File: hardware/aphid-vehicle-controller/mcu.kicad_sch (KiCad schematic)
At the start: 2 parts, among them J2 Conn_ST_STDC14, U1 STM32F405RGTx

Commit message: worked on schematic
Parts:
- added Y1: Crystal, symbol Device:Crystal
- J2: value Conn_ST_STDC14 -> MAIN_DEBUG
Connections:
- net GND: now reaches J2.11 (GNDDetect)
- net GND: now also J2.5 (GND), J2.7 (GND)
- net MAIN_NRST: now reaches J2.12 (~{RST})
- net MAIN_DBG_RX: now reaches J2.13 (VCP_RX)
- net MAIN_DBG_TX: now reaches J2.14 (VCP_TX)
- net +3.3V: now reaches J2.3 (VCC)
- net MAIN_SWDIO: now reaches J2.4 (JTMS/SWDIO)
- net MAIN_SWCLK: now reaches J2.6 (JCLK/SWCLK)
- net MAIN_SWO: now reaches J2.8 (JTDO/SWO)

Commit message: more work on pcb
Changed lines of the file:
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@@
+		)
+	)
+	(hierarchical_label "POWER_KEEPALIVE"
+		(shape output)
+		(at 217.17 43.18 0)
+		(fields_autoplaced yes)
+		(effects
+			(font
+				(size 1.27 1.27)
+			)
+			(justify left)
 		)
 	)

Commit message: worked on VCM
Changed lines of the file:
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@@
 		)
 	)
-	(hierarchical_label "ACC2_FILTERED"
+	(hierarchical_label "DIR_R"
 		(shape input)
-		(at 190.5 138.43 0)
+		(at 182.88 118.11 0)
+		(fields_autoplaced yes)
+		(effects
+			(font
+				(size 1.27 1.27)
+			)
+			(justify left)
+		)
+	)
+	(hierarchical_label "MONITOR_UART_TX"
+		(shape output)
+		(at 45.72 92.71 0)
+		(fields_autoplaced yes)
+		(effects
+			(font
+				(size 1.27 1.27)
+			)
+			(justify left)
+		)
+	)
+	(hierarchical_label "MONITOR_UART_RX"
+		(shape input)
+		(at 45.72 96.52 0)
+		(fields_autoplaced yes)
+		(effects
+			(font
+				(size 1.27 1.27)
+			)
+			(justify left)
+		)
+	)
+	(hierarchical_label "BRAKE"
+		(shape input)
+		(at 182.88 106.68 0)
+		(fields_autoplaced yes)
+		(effects
+			(font
+				(size 1.27 1.27)
+			)
+			(justify left)
+		)
+	)
+	(hierarchical_label "CRANK_SENSE"
+		(shape input)
+		(at 195.58 130.81 0)
 		(fields_autoplaced yes)
 		(effects
@@
 		(shape output)
 		(at 217.17 43.18 0)
+		(fields_autoplaced yes)
+		(effects
+			(font
+				(size 1.27 1.27)
+			)
+			(justify left)
+		)
+	)
+	(hierarchical_label "DIR_F"
+		(shape input)
+		(at 182.88 113.03 0)
 		(fields_autoplaced yes)
 		(effects
@@
 		)
 	)
-	(hierarchical_label "UPPER_CONTACTOR_ENABLE"
-		(shape output)
-		(at 201.93 114.3 0)
-		(fields_autoplaced yes)
-		(effects
-			(font
-				(size 1.27 1.27)
-			)
-			(justify left)
-		)
-	)
 	(hierarchical_label "CAN1_RX"
 		(shape input)
@@
 		)
 	)
-	(hierarchical_label "ACC1_FILTERED"
+	(hierarchical_label "ACC"
 		(shape input)
 		(at 176.53 91.44 0)
@@
 		)
 	)
-	(hierarchical_label "LOWER_CONTACTOR_ENABLE"
-		(shape output)
-		(at 201.93 116.84 0)
+	(hierarchical_label "IGNITION_SENSE"
+		(shape input)
+		(at 215.9 116.84 0)
 		(fields_autoplaced yes)
 		(effects
@@
 		)
 	)
-	(hierarchical_label "PRECHARGE_ENABLE"
-		(shape output)
-		(at 203.2 109.22 0)
+	(hierarchical_label "VIN_SENSE"
+		(shape input)
+		(at 215.9 114.3 0)
 		(fields_autoplaced yes)
 		(effects

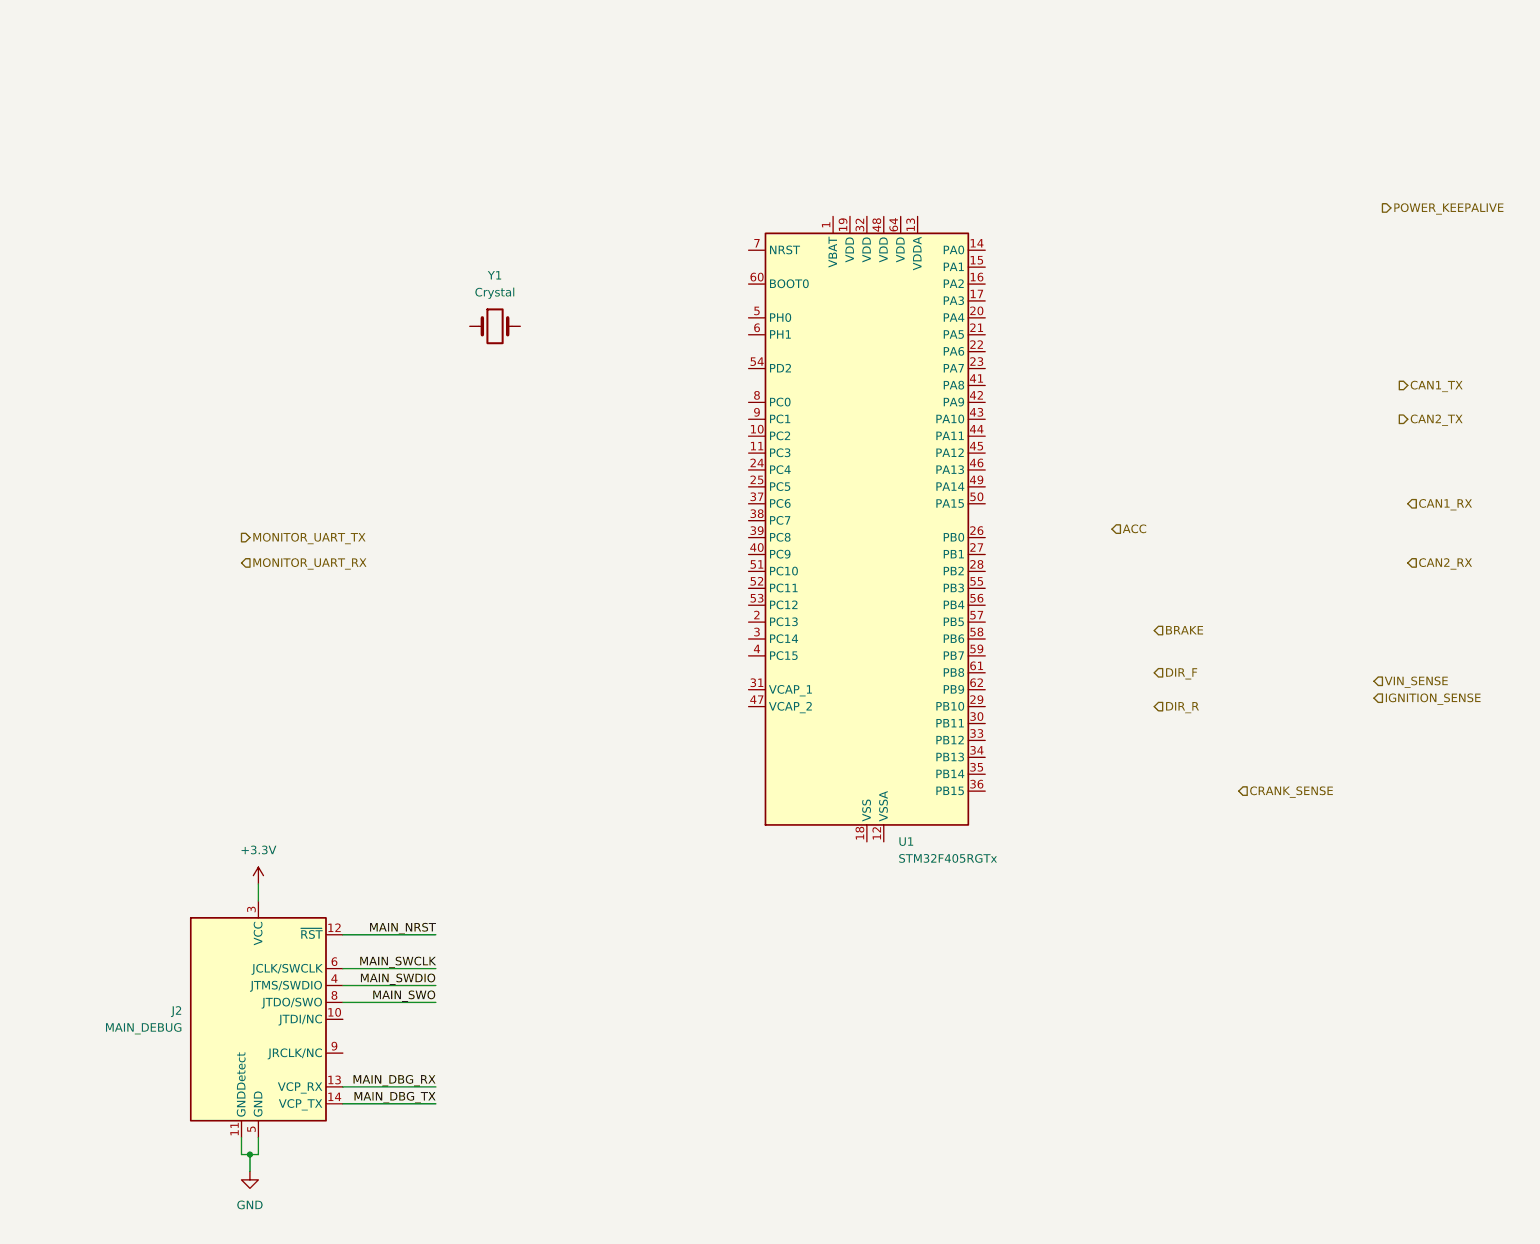
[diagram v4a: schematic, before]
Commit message: feat: changed to STM32G4xx series MCU
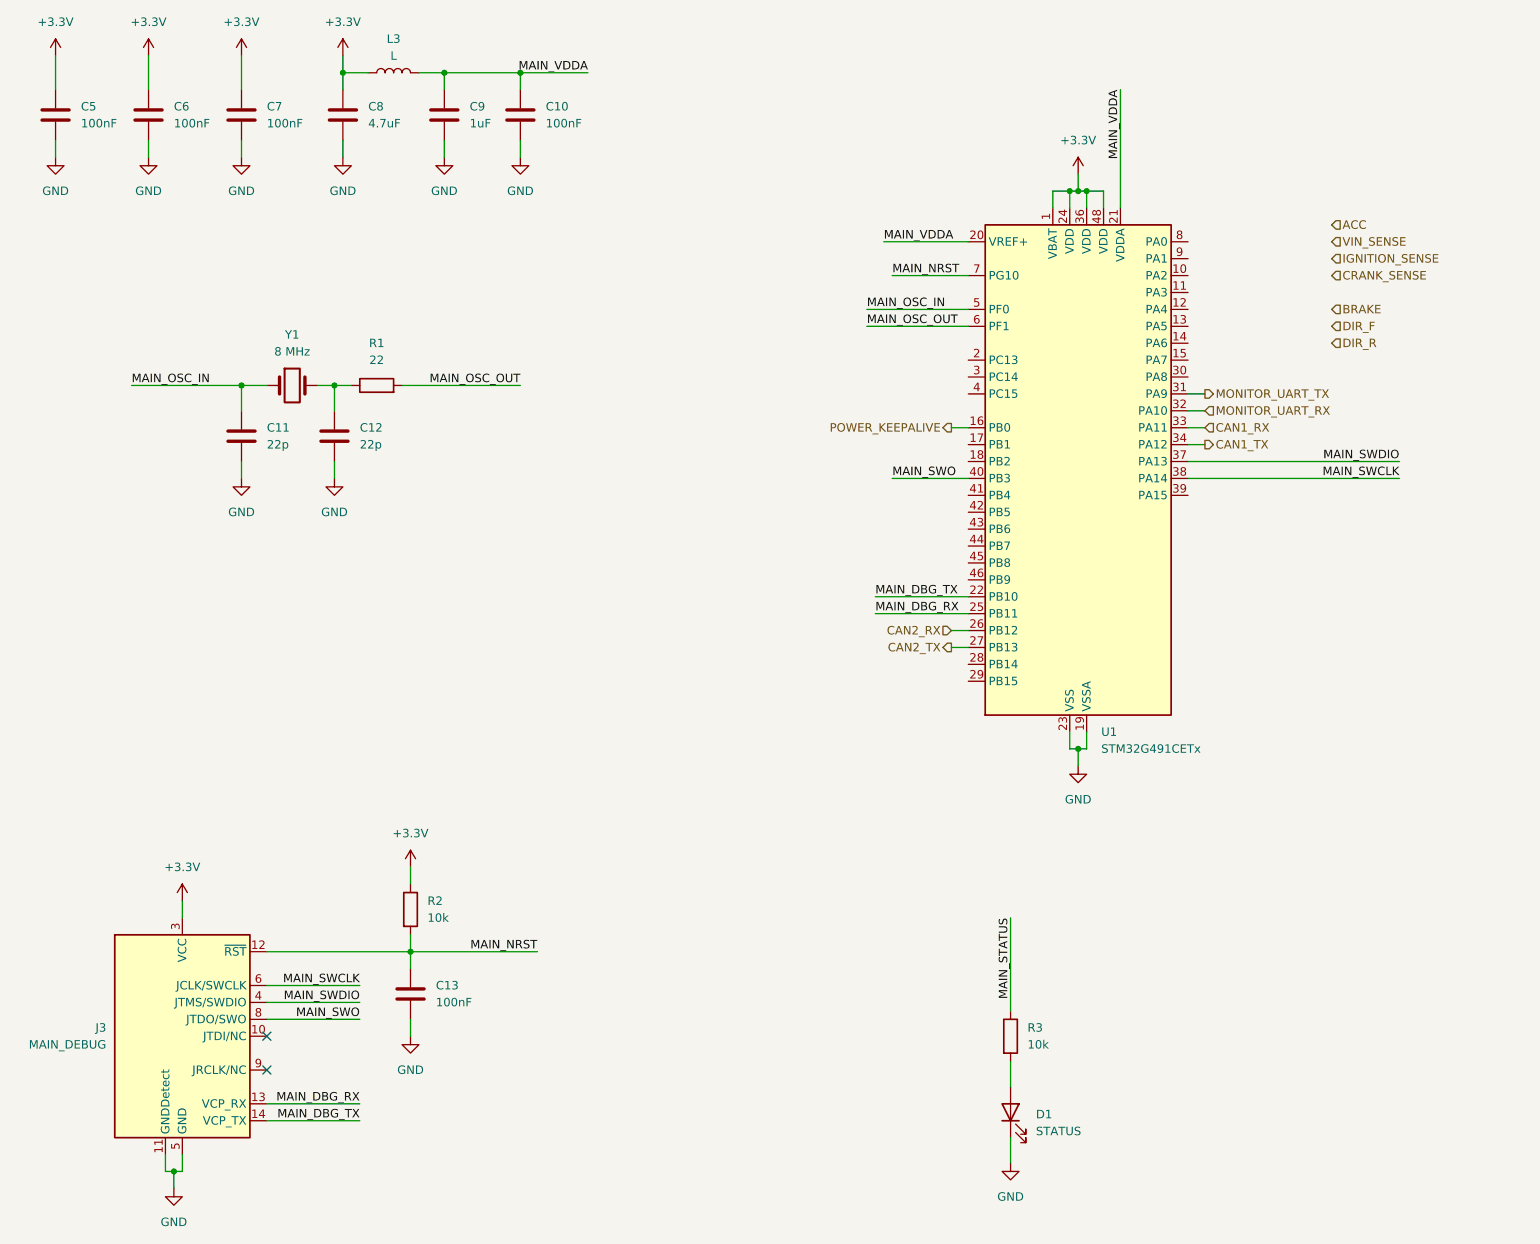
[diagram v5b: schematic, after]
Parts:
- removed U1: STM32F405RGTx, Package_QFP:LQFP-64_10x10mm_P0.5mm, symbol MCU_ST_STM32F4:STM32F405RGTx
- added C10, C13, C5, C6, C7: 100nF, Capacitor_SMD:C_0603_1608Metric, symbol Device:C
- added C11, C12: 22p, Capacitor_SMD:C_0603_1608Metric, symbol Device:C
- added C8: 4.7uF, Capacitor_SMD:C_0805_2012Metric, symbol Device:C
- added C9: 1uF, Capacitor_SMD:C_0603_1608Metric, symbol Device:C
- added D1: STATUS, LED_SMD:LED_0603_1608Metric, symbol Device:LED
- added L3: L, Inductor_SMD:L_0805_2012Metric, symbol Device:L
- added R1: 22, Resistor_SMD:R_0603_1608Metric, symbol Device:R
- added R2, R3: 10k, Resistor_SMD:R_0603_1608Metric, symbol Device:R
- added U1: STM32G491CETx, Package_QFP:LQFP-48_7x7mm_P0.5mm, symbol MCU_ST_STM32G4:STM32G491CETx
- Y1: value Crystal -> 8 MHz; footprint (none) -> aphid:ABM3-x.xxxMHZ-D2Y-T
- renumbered J2 to J3
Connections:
- net +3.3V: now also C5.1, C6.1, C7.1, C8.1, L3.1, R2.1, U1.1 (VBAT), U1.24 (VDD), U1.36 (VDD), U1.48 (VDD)
- net CAN1_RX: now also U1.33 (PA11)
- net CAN1_TX: now also U1.34 (PA12)
- net CAN2_RX: now also U1.26 (PB12)
- net CAN2_TX: now also U1.27 (PB13)
- net GND: now also C10.2, C11.2, C12.2, C13.2, C5.2, C6.2, C7.2, C8.2, C9.2, D1.1 (K), U1.19 (VSSA), U1.23 (VSS), U1.35 (VSS), U1.47 (VSS)
- net MAIN_DBG_RX: now also U1.25 (PB11)
- net MAIN_DBG_TX: now also U1.22 (PB10)
- net MAIN_NRST: now also C13.1, R2.2, U1.7 (PG10)
- net MAIN_SWCLK: now also U1.38 (PA14)
- net MAIN_SWDIO: now also U1.37 (PA13)
- net MAIN_SWO: now also U1.40 (PB3)
- net MONITOR_UART_RX: now also U1.32 (PA10)
- net MONITOR_UART_TX: now also U1.31 (PA9)
- net POWER_KEEPALIVE: now also U1.16 (PB0)
- net MAIN_OSC_IN: now reaches Y1.1
- net MAIN_OSC_IN: now also C11.1, U1.5 (PF0)
- net at Y1.2: now also C12.1, R1.1
- new net: D1.2 (A), R3.2
- new net MAIN_OSC_OUT: R1.2, U1.6 (PF1)
- new net MAIN_STATUS: R3.1
- new net MAIN_VDDA: C10.1, C9.1, L3.2, U1.20 (VREF+), U1.21 (VDDA)
- no-connect marks 0 -> 2
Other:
- moved on the sheet: J3, Y1

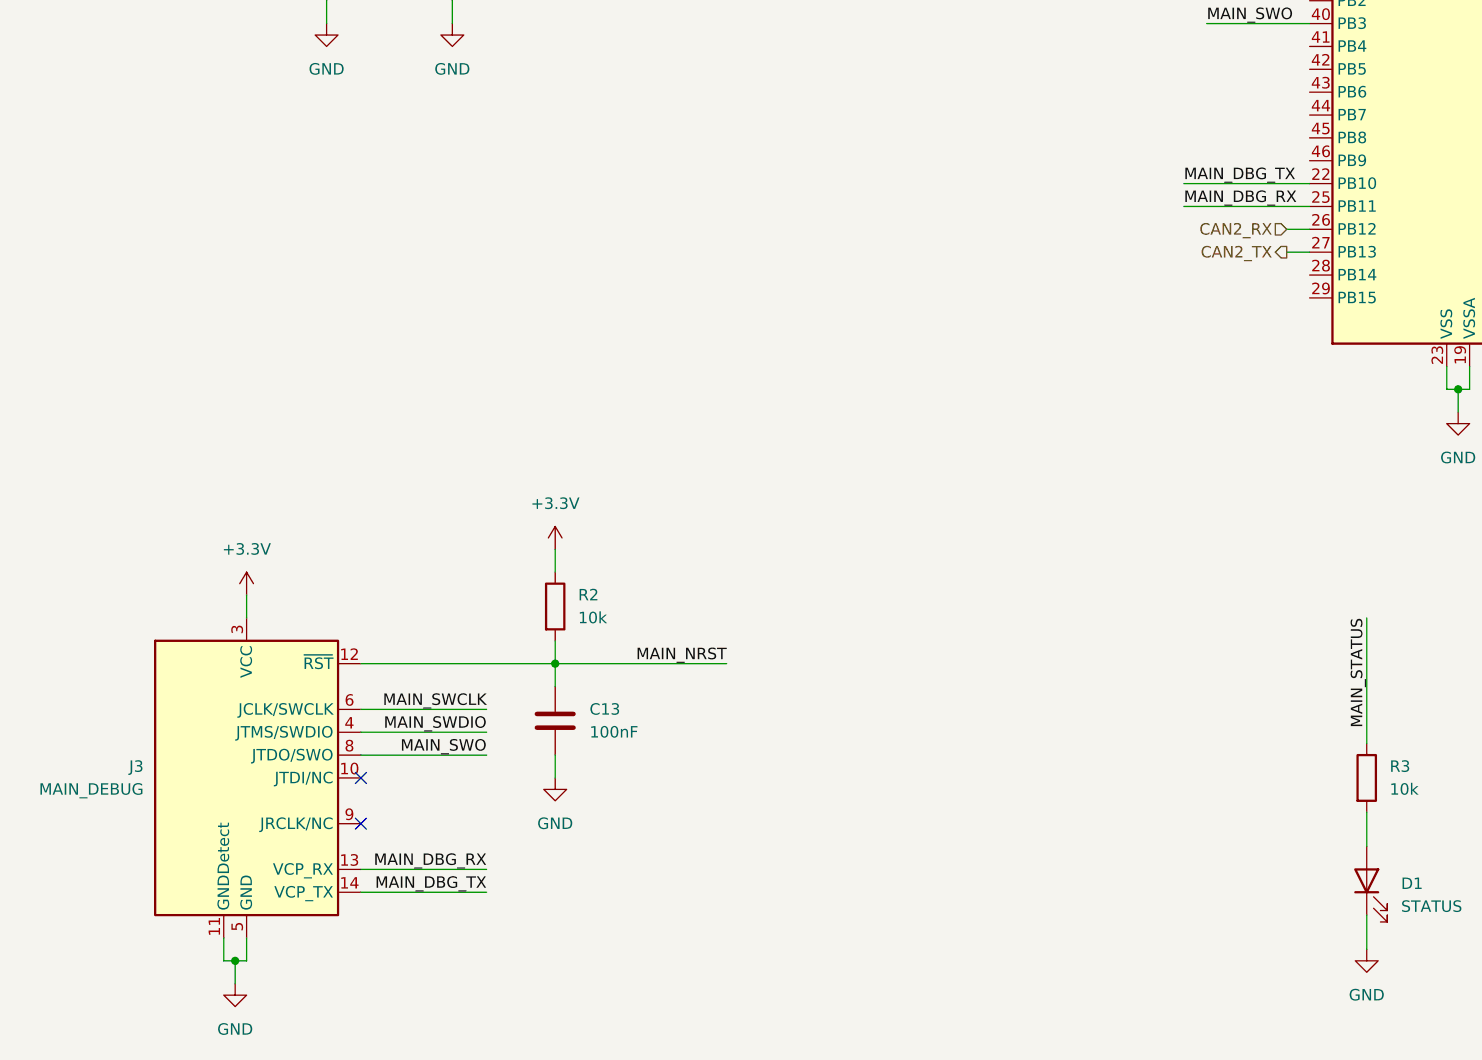
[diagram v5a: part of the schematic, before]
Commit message: Changed debug connector to tagconnect
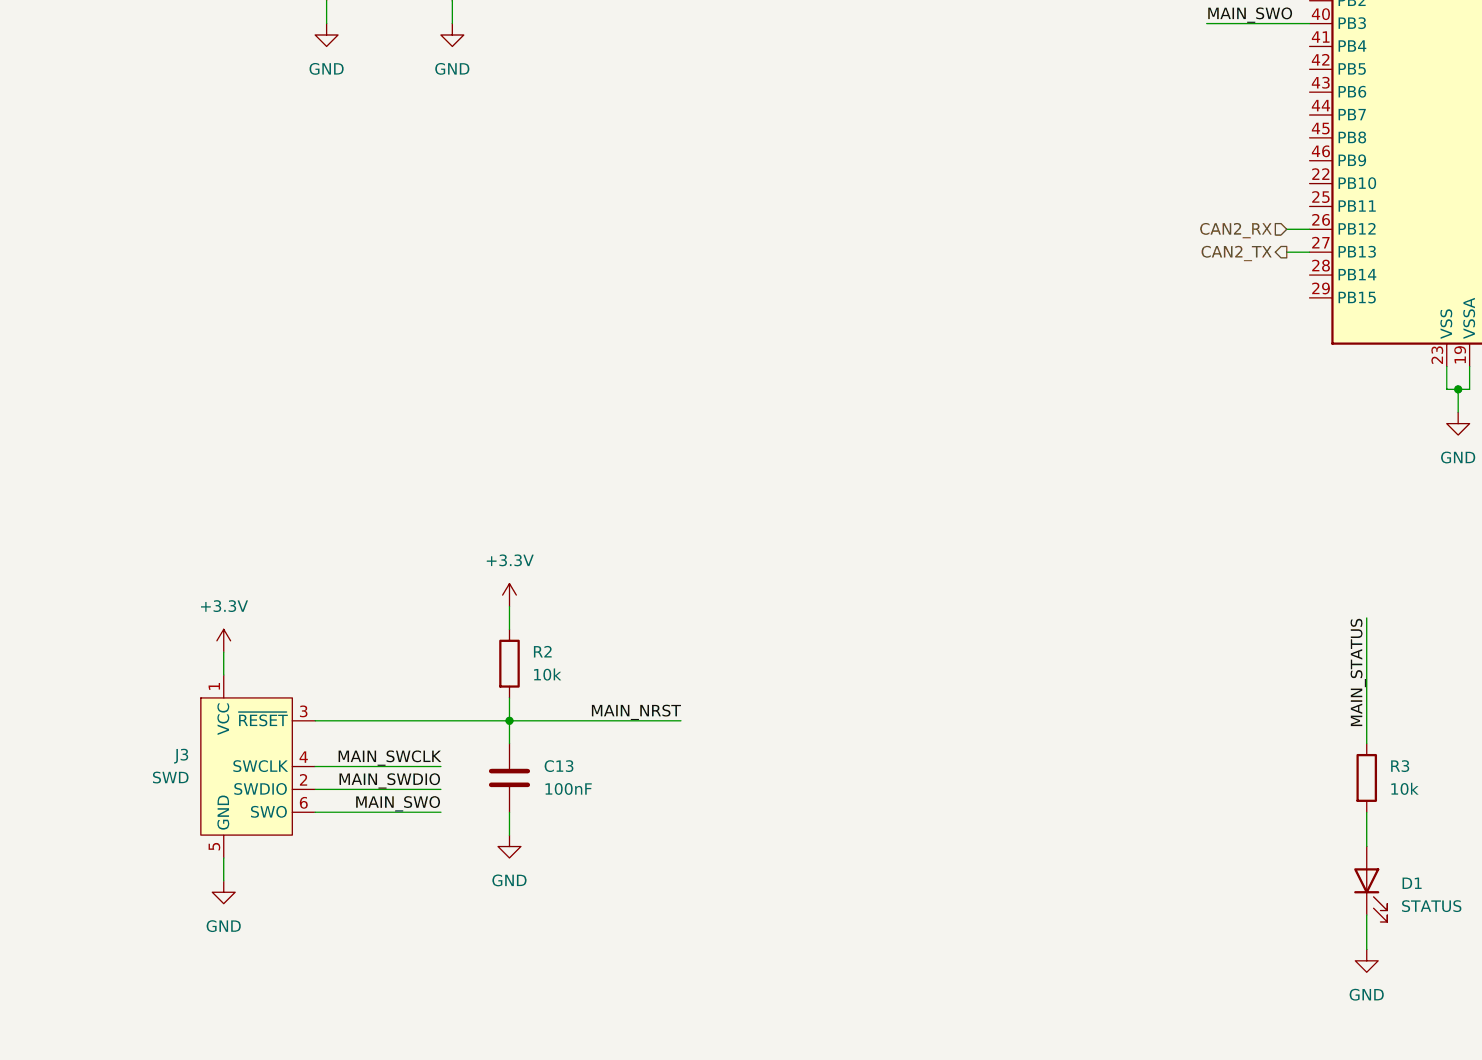
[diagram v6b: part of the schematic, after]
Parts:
- removed J3: MAIN_DEBUG, Connector_PinHeader_1.27mm:PinHeader_2x07_P1.27mm_Vertical_SMD, symbol Connector:Conn_ST_STDC14
- added J3: SWD, Connector:Tag-Connect_TC2030-IDC-FP_2x03_P1.27mm_Vertical, symbol Connector:Conn_ARM_SWD_TagConnect_TC2030
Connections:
- net +3.3V: now also J3.1 (VCC)
- net GND: now also J3.5 (GND)
- net MAIN_NRST: now also J3.3 (~{RESET})
- net MAIN_SWCLK: now also J3.4 (SWCLK)
- net MAIN_SWDIO: now also J3.2 (SWDIO)
- net MAIN_SWO: now also J3.6 (SWO)
- net MAIN_DBG_RX: no longer names the net of U1.25 (PB11)
- net MAIN_DBG_TX: no longer names the net of U1.22 (PB10)
- no-connect marks 2 -> 0
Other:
- moved on the sheet: C13, R2

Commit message: Worked on VC PCB
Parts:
- removed J3: SWD, Connector:Tag-Connect_TC2030-IDC-FP_2x03_P1.27mm_Vertical, symbol Connector:Conn_ARM_SWD_TagConnect_TC2030
- added J3: MAIN_DEBUG, Connector_PinHeader_1.27mm:PinHeader_2x07_P1.27mm_Vertical_SMD, symbol Connector:Conn_ST_STDC14
- added J4: SWD, Connector:Tag-Connect_TC2030-IDC-FP_2x03_P1.27mm_Vertical, symbol Connector:Conn_ARM_SWD_TagConnect_TC2030
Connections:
- net +3.3V: now also J3.3 (VCC), J4.1 (VCC)
- net GND: now also J3.11 (GNDDetect), J3.5 (GND), J3.7 (GND), J4.5 (GND)
- net MAIN_NRST: now also J3.12 (~{RST}), J4.3 (~{RESET})
- net MAIN_SWCLK: now also J3.6 (JCLK/SWCLK), J4.4 (SWCLK)
- net MAIN_SWDIO: now also J3.4 (JTMS/SWDIO), J4.2 (SWDIO)
- net MAIN_SWO: now also J3.8 (JTDO/SWO), J4.6 (SWO)
- net MAIN_DBG_TX: now reaches U1.22 (PB10)
- net MAIN_DBG_TX: now also J3.14 (VCP_TX)
- net MAIN_DBG_RX: now reaches U1.25 (PB11)
- net MAIN_DBG_RX: now also J3.13 (VCP_RX)
- no-connect marks 0 -> 2
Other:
- moved on the sheet: C13, R2
